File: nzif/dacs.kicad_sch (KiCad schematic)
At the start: 1 part, among them U5 ADAU1966AWBSTZ

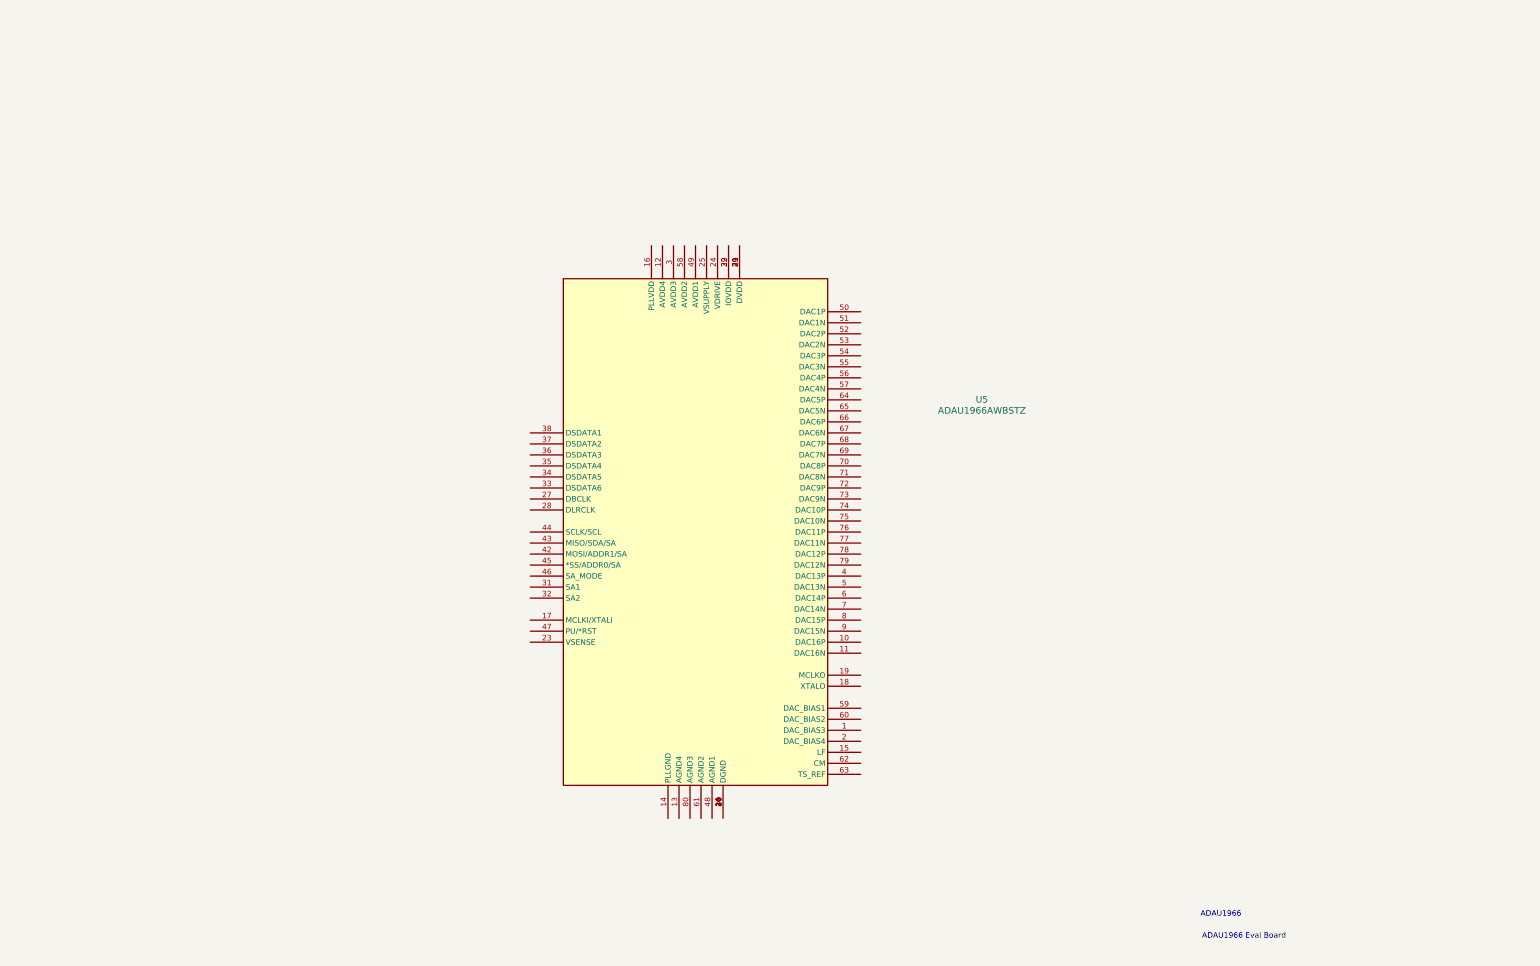
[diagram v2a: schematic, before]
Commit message: Continue wiring DAC (Ref #29)
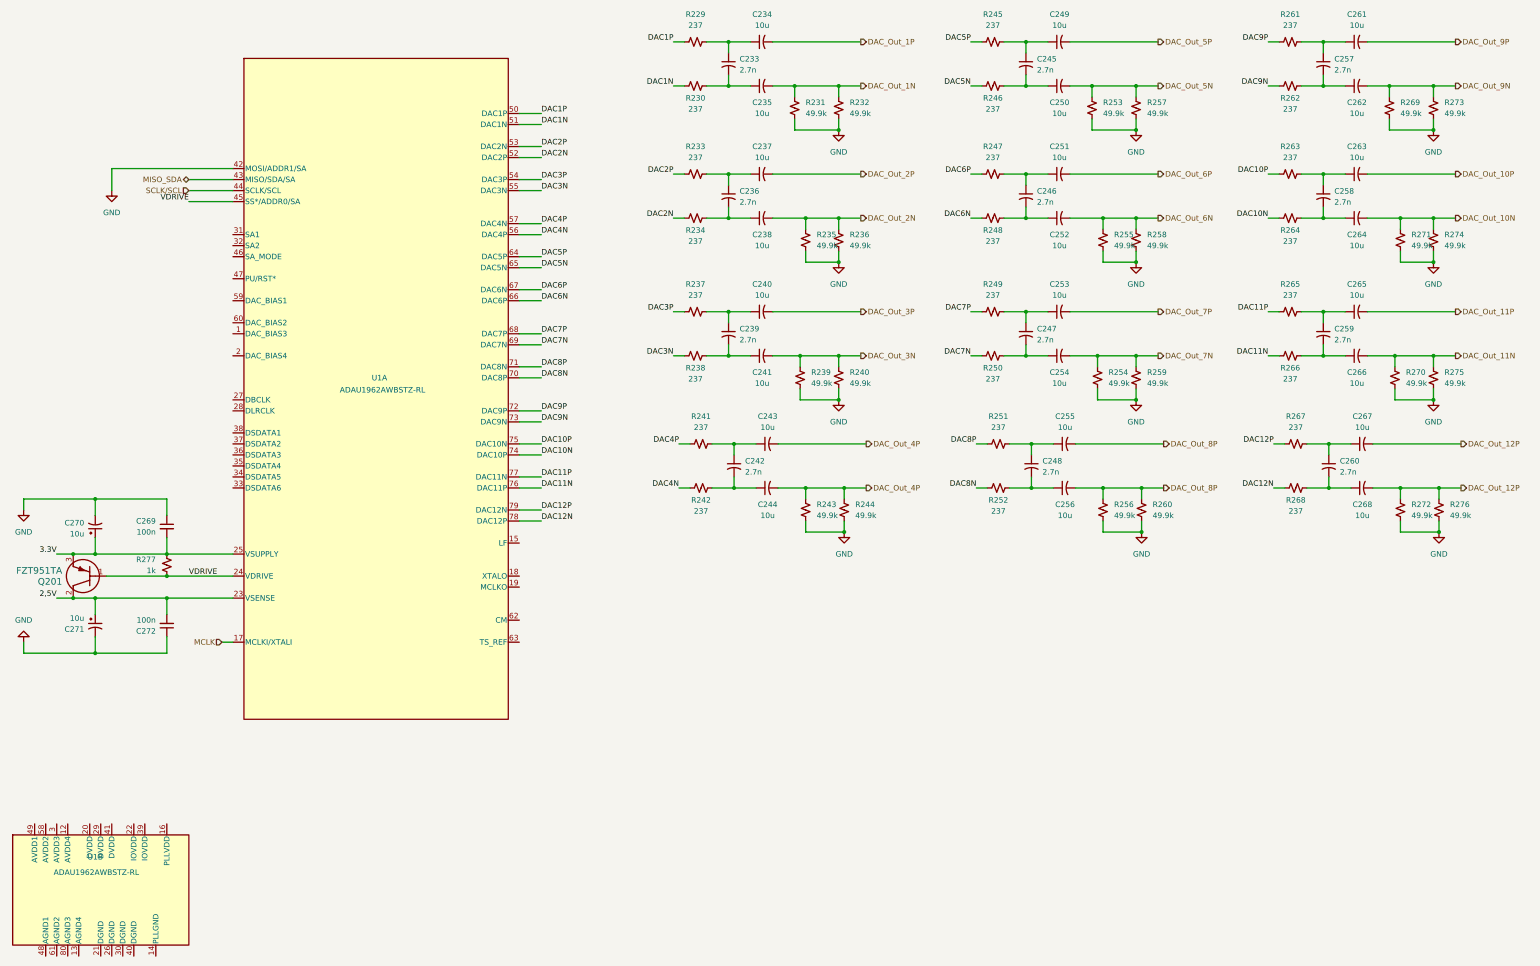
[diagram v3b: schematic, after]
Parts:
- removed U5: ADAU1966AWBSTZ, nzif_footprints:ST_80_2_ADI, symbol nzif_radio_symbol_library:ADAU1966AWBSTZ
- added C233, C236, C239, C242, C245, C246, C247, C248, C257, C258, C259, C260: 2.7n, symbol Device:C_Small_US
- added C234, C235, C237, C238, C240, C241, C243, C244, C249, C250, C251, C252, C253, C254, C255, C256, C261, C262, C263, C264, C265, C266, C267, C268: 10u, symbol Device:C_Small_US
- added C269, C272: 100n, symbol Device:C_Small
- added C270, C271: 10u, symbol Device:C_Polarized_Small_US
- added Q201: FZT951TA, nzif_footprints:SOT223-FZT690B-DN_DIO, symbol nzif_radio_symbol_library:FZT951TA
- added R229, R230, R233, R234, R237, R238, R241, R242, R245, R246, R247, R248, R249, R250, R251, R252, R261, R262, R263, R264, R265, R266, R267, R268: 237, symbol Device:R_Small_US
- added R231, R232, R235, R236, R239, R240, R243, R244, R253, R254, R255, R256, R257, R258, R259, R260, R269, R270, R271, R272, R273, R274, R275, R276: 49.9k, symbol Device:R_Small_US
- added R277: 1k, symbol Device:R_Small_US
- added U1: ADAU1962AWBSTZ-RL, nzif_footprints:ST_80_2_ADI, symbol nzif_radio_symbol_library:ADAU1962AWBSTZ-RL
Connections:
- new net: C247.2, C254.1, R250.2
- new net: C247.1, C253.1, R249.2
- new net: C242.2, C244.1, R242.2
- new net: C248.2, C256.1, R252.2
- new net: C260.2, C268.1, R268.2
- new net: C257.2, C262.1, R262.2
- new net: C258.2, C264.1, R264.2
- new net: C236.1, C237.1, R233.2
- new net: C236.2, C238.1, R234.2
- new net: C245.2, C250.1, R246.2
- new net: C248.1, C255.1, R251.2
- new net: C239.2, C241.1, R238.2
- new net: C246.2, C252.1, R248.2
- new net: C233.2, C235.1, R230.2
- new net: C257.1, C261.1, R261.2
- new net: C239.1, C240.1, R237.2
- new net: C259.2, C266.1, R266.2
- new net: U1.10 (NC), U1.11 (NC), U1.4 (NC), U1.5 (NC), U1.6 (NC), U1.7 (NC), U1.8 (NC), U1.9 (NC)
- new net: C258.1, C263.1, R263.2
- new net: C259.1, C265.1, R265.2
- new net: C246.1, C251.1, R247.2
- new net: C242.1, C243.1, R241.2
- new net: C260.1, C267.1, R267.2
- new net: C245.1, C249.1, R245.2
- new net: C233.1, C234.1, R229.2
- new net 2,5V: C271.1, C272.2, Q201.2, U1.23 (VSENSE)
- new net 3.3V: C269.2, C270.1, Q201.3, R277.1, U1.25 (VSUPPLY)
- new net DAC10N: R264.1, U1.74 (DAC10P)
- new net DAC10P: R263.1, U1.75 (DAC10N)
- new net DAC11N: R266.1, U1.76 (DAC11P)
- new net DAC11P: R265.1, U1.77 (DAC11N)
- new net DAC12N: R268.1, U1.78 (DAC12P)
- new net DAC12P: R267.1, U1.79 (DAC12N)
- new net DAC1N: R230.1, U1.51 (DAC1N)
- new net DAC1P: R229.1, U1.50 (DAC1P)
- new net DAC2N: R234.1, U1.52 (DAC2P)
- new net DAC2P: R233.1, U1.53 (DAC2N)
- new net DAC3N: R238.1, U1.55 (DAC3N)
- new net DAC3P: R237.1, U1.54 (DAC3P)
- new net DAC4N: R242.1, U1.56 (DAC4P)
- new net DAC4P: R241.1, U1.57 (DAC4N)
- new net DAC5N: R246.1, U1.65 (DAC5N)
- new net DAC5P: R245.1, U1.64 (DAC5P)
- new net DAC6N: R248.1, U1.66 (DAC6P)
- new net DAC6P: R247.1, U1.67 (DAC6N)
- new net DAC7N: R250.1, U1.69 (DAC7N)
- new net DAC7P: R249.1, U1.68 (DAC7P)
- new net DAC8N: R252.1, U1.70 (DAC8P)
- new net DAC8P: R251.1, U1.71 (DAC8N)
- new net DAC9N: R262.1, U1.73 (DAC9N)
- new net DAC9P: R261.1, U1.72 (DAC9P)
- new net DAC_Out_10N: C264.2, R271.2, R274.2
- new net DAC_Out_10P: C263.2
- new net DAC_Out_11N: C266.2, R270.2, R275.2
- new net DAC_Out_11P: C265.2
- new net DAC_Out_12P: C267.2, C268.2, R272.2, R276.2
- new net DAC_Out_1N: C235.2, R231.2, R232.2
- new net DAC_Out_1P: C234.2
- new net DAC_Out_2N: C238.2, R235.2, R236.2
- new net DAC_Out_2P: C237.2
- new net DAC_Out_3N: C241.2, R239.2, R240.2
- new net DAC_Out_3P: C240.2
- new net DAC_Out_4P: C243.2, C244.2, R243.2, R244.2
- new net DAC_Out_5N: C250.2, R253.2, R257.2
- new net DAC_Out_5P: C249.2
- new net DAC_Out_6N: C252.2, R255.2, R258.2
- new net DAC_Out_6P: C251.2
- new net DAC_Out_7N: C254.2, R254.2, R259.2
- new net DAC_Out_7P: C253.2
- new net DAC_Out_8P: C255.2, C256.2, R256.2, R260.2
- new net DAC_Out_9N: C262.2, R269.2, R273.2
- new net DAC_Out_9P: C261.2
- new net GND: C269.1, C270.2, C271.2, C272.1, R231.1, R232.1, R235.1, R236.1, R239.1, R240.1, R243.1, R244.1, R253.1, R254.1, R255.1, R256.1, R257.1, R258.1, R259.1, R260.1, R269.1, R270.1, R271.1, R272.1, R273.1, R274.1, R275.1, R276.1, U1.42 (MOSI/ADDR1/SA)
- new net MCLK: U1.17 (MCLKI/XTALI)
- new net MISO_SDA: U1.43 (MISO/SDA/SA)
- new net SCLK/SCL: U1.44 (SCLK/SCL)
- new net VDRIVE: Q201.1, R277.2, U1.24 (VDRIVE), U1.45 (SS*/ADDR0/SA)
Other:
- note removed: "ADAU1966"
- note removed: "ADAU1966 Eval Board"

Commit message: add  PCS2P2309
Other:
- note added: "ADAU 1962 EVAL Board"
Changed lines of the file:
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@@
 		(company "Andy McCann KA3KAF and Doug McCann KA3KAG")
+	)
+	(text "ADAU 1962 EVAL Board"
+		(exclude_from_sim no)
+		(at 357.632 228.854 0)
+		(effects
+			(font
+				(size 5.08 5.08)
+				(thickness 1.016)
+				(bold yes)
+			)
+			(href "https://www.analog.com/media/en/technical-documentation/user-guides/UG-416.pdf")
+		)
 	)
 	(junction

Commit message: Wire DAC (Ref #29)
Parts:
- added C273, C274, C275, C276: 470n, symbol Device:C_Small_US
- added C277, C279, C281, C283, C285, C287, C289, C291, C293, C295, C297, C299: 10n, symbol Device:C_Small_US
- added C278, C280, C282, C284, C286, C288, C290, C292, C294, C296, C298, C300: .1u, symbol Device:C_Small_US
- added C301: 150p, symbol Device:C_Small_US
- added C302: 2.2n, symbol Device:C_Small_US
- added R278: 3.32k, symbol Device:R_Small_US
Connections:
- net GND: now also U1.13 (AGND4), U1.14 (PLLGND), U1.21 (DGND), U1.26 (DGND), U1.30 (DGND), U1.31 (SA1), U1.32 (SA2), U1.40 (DGND), U1.46 (SA_MODE), U1.48 (AGND1), U1.61 (AGND2), U1.80 (AGND3), C274.2, C275.2, C277.2, C278.2, C279.2, C280.2, C281.2, C282.2, C283.2, C284.2, C285.2, C286.2, C287.2, C288.2, C289.2, C290.2, C291.2, C292.2, C293.2, C294.2, C295.2, C296.2, C297.2, C298.2, C299.2, C300.2
- net AVDD3: now reaches U1.12 (AVDD4)
- net AVDD3: now also U1.3 (AVDD3), C276.2, C285.1, C286.1, C289.1, C290.1
- net 2.5: now reaches U1.16 (PLLVDD)
- net 2.5: now also C299.1, C300.1, C302.2, R278.2
- net DVDD: now reaches U1.20 (DVDD)
- net DVDD: now also U1.29 (DVDD), U1.41 (DVDD), C277.1, C278.1, C283.1, C284.1, C287.1, C288.1
- net IOVDD: now reaches U1.22 (IOVDD)
- net IOVDD: now also U1.39 (IOVDD), C291.1, C292.1, C297.1, C298.1
- net AVDD1: now reaches U1.49 (AVDD1)
- net AVDD1: now also C279.1, C280.1
- net AVDD2: now reaches U1.58 (AVDD2)
- net AVDD2: now also C273.2, C281.1, C282.1
- net at U1.1 (DAC_BIAS3): now also C275.1
- net at U1.15 (LF): now also C301.1, C302.1
- net at U1.2 (DAC_BIAS4): now also C276.1
- net BCLK_OUT1: now reaches U1.27 (DBCLK)
- net LRCLK_OUT1: now reaches U1.28 (DLRCLK)
- net TDM1_SDIN_DAC: now reaches U1.38 (DSDATA1)
- net at U1.59 (DAC_BIAS1): now also C273.1
- net at U1.60 (DAC_BIAS2): now also C274.1
- net at U1.62 (CM): now also C293.1, C294.1
- net at U1.63 (TS_REF): now also C295.1, C296.1
- net 2,5V renamed 2.5V
- new net: C301.2, R278.1
- no-connect marks 0 -> 7
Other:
- note added: "DAC_Out_9x to 12x go to a header on the top sheet"
- moved on the sheet: U1B

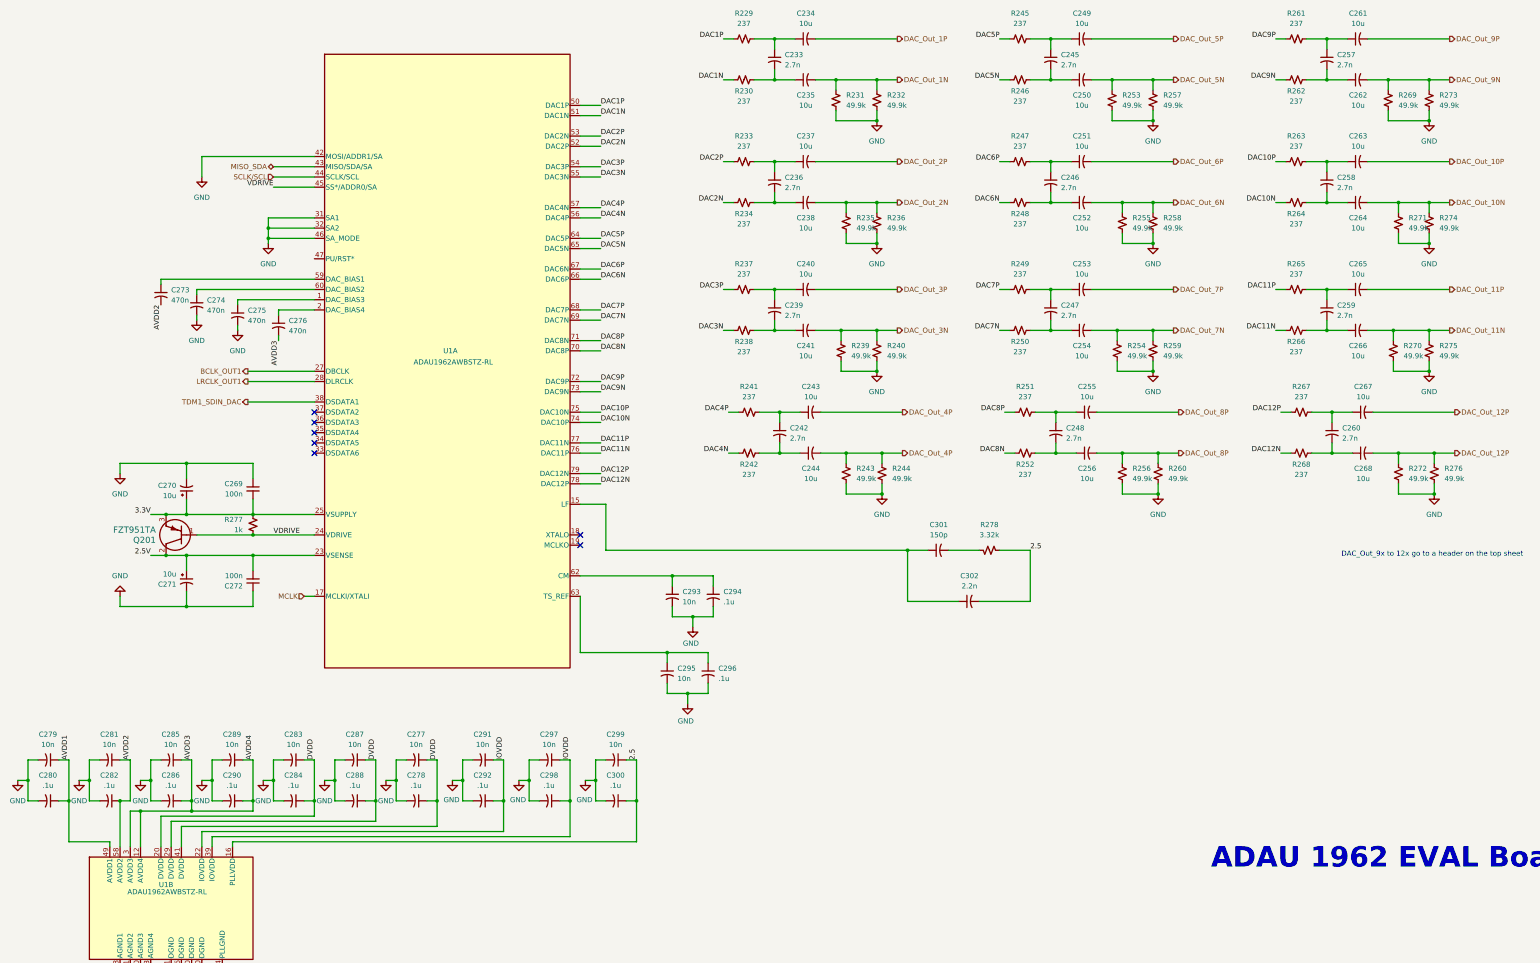
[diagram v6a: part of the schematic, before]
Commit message: reordered sheets - annotate sheets - set all to no sim
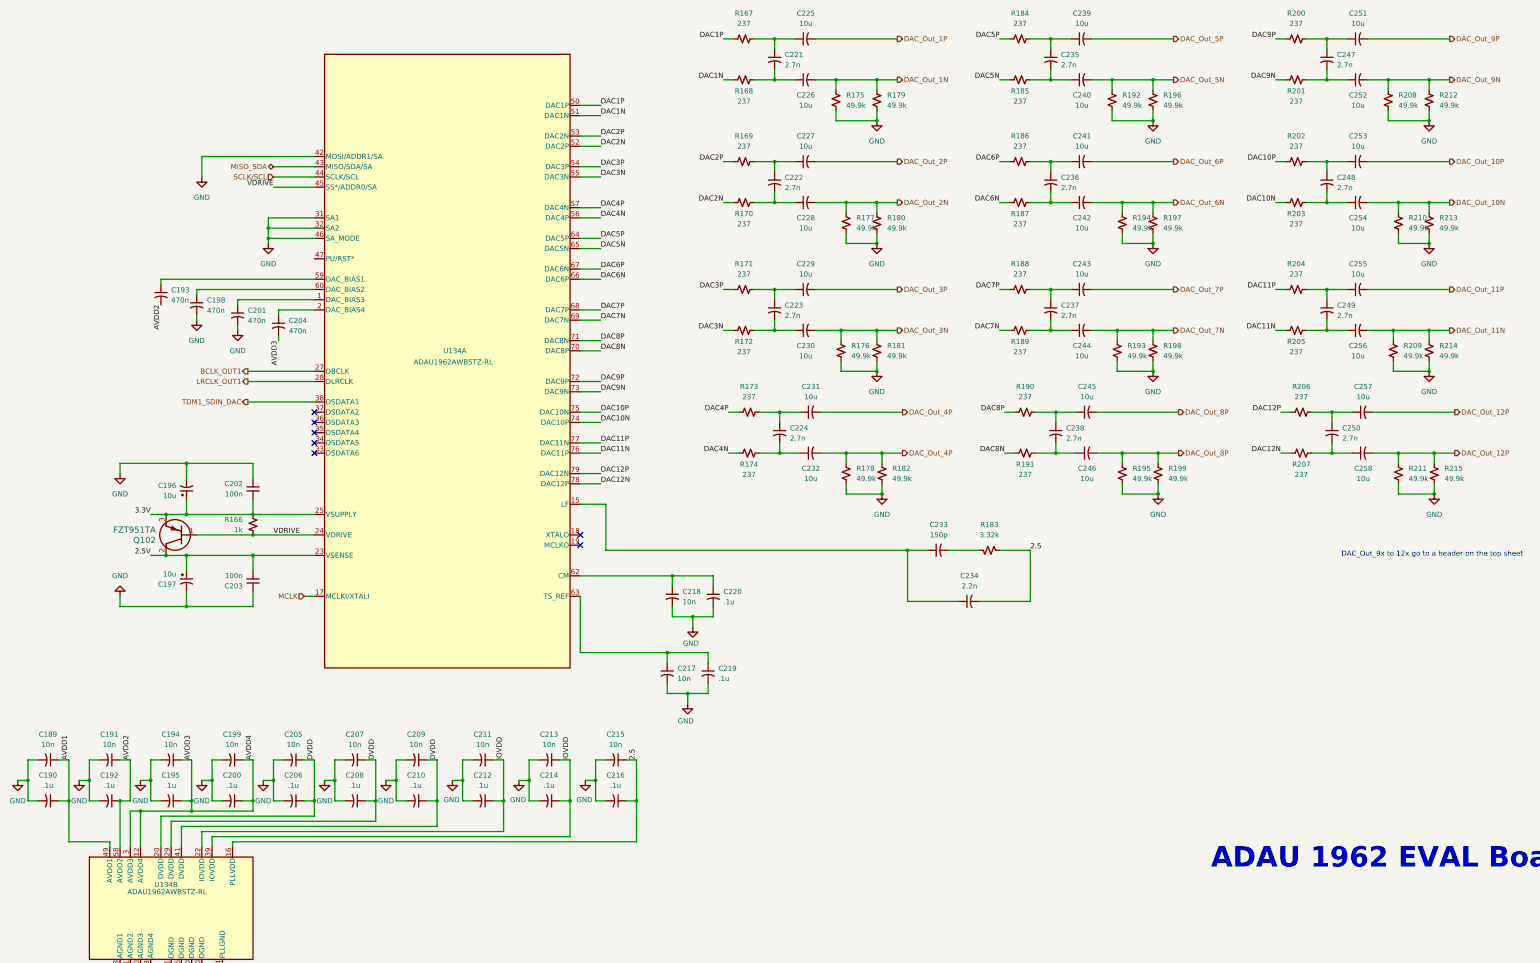
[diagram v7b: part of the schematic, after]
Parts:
- renumbered C279 to C189, C280 to C190, C281 to C191, C282 to C192, C273 to C193, C285 to C194, C286 to C195, C270 to C196, C271 to C197, C274 to C198, C289 to C199, C290 to C200, C275 to C201, C269 to C202, C272 to C203, C276 to C204, C283 to C205, C284 to C206, C287 to C207, C288 to C208, C277 to C209, C278 to C210, C291 to C211, C292 to C212, C297 to C213, C298 to C214, C299 to C215, C300 to C216, C295 to C217, C293 to C218, C296 to C219, C294 to C220, C233 to C221, C236 to C222, C239 to C223, C242 to C224, C234 to C225, C235 to C226, C237 to C227, C238 to C228, C240 to C229, C241 to C230, C243 to C231, C244 to C232, C301 to C233, C302 to C234, C245 to C235, C246 to C236, C247 to C237, C248 to C238, C249 to C239, C250 to C240, C251 to C241, C252 to C242, C253 to C243, C254 to C244, C255 to C245, C256 to C246, C257 to C247, C258 to C248, C259 to C249, C260 to C250, C261 to C251, C262 to C252, C263 to C253, C264 to C254, C265 to C255, C266 to C256, C267 to C257, C268 to C258, Q201 to Q102, R277 to R166, R229 to R167, R230 to R168, R233 to R169, R234 to R170, R237 to R171, R238 to R172, R241 to R173, R242 to R174, R231 to R175, R239 to R176, R235 to R177, R243 to R178, R232 to R179, R236 to R180, R240 to R181, R244 to R182, R278 to R183, R245 to R184, R246 to R185, R247 to R186, R248 to R187, R249 to R188, R250 to R189, R251 to R190, R252 to R191, R253 to R192, R254 to R193, R255 to R194, R256 to R195, R257 to R196, R258 to R197, R259 to R198, R260 to R199, R261 to R200, R262 to R201, R263 to R202, R264 to R203, R265 to R204, R266 to R205, R267 to R206, R268 to R207, R269 to R208, R270 to R209, R271 to R210, R272 to R211, R273 to R212, R274 to R213, R275 to R214, R276 to R215, U1 to U134
